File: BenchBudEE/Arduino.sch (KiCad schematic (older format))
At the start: 0 parts

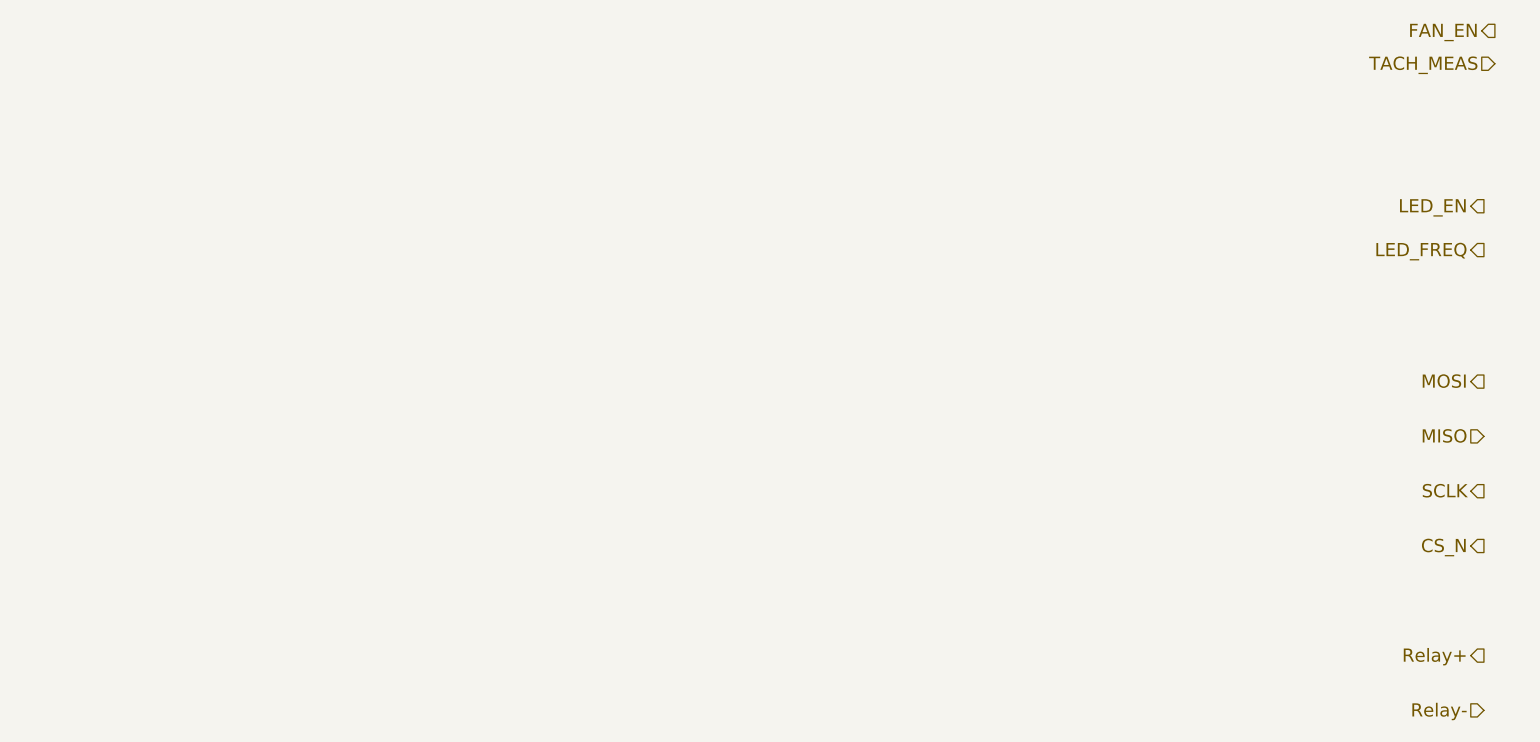
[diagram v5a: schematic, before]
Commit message: Arduino block diagram
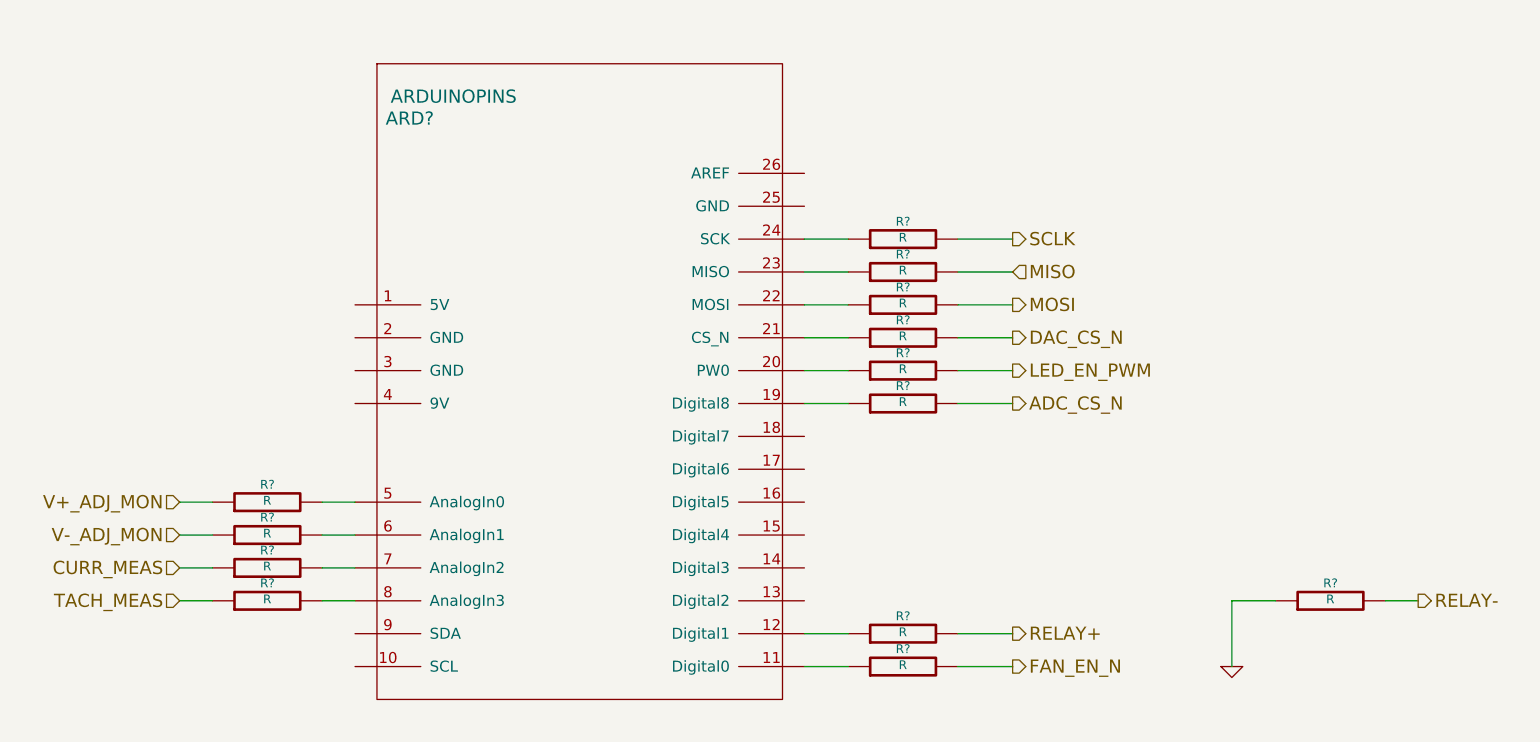
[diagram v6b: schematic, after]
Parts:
- added ARD?: ARDUINOPINS, symbol ARDUINOPINS
- added R? (x13): R, ~, symbol R
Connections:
- net MISO: now also R?.2
- net MOSI: now also R?.2
- net SCLK: now also R?.2
- net TACH_MEAS: now also R?.1
- new net: ARD?.11 (Digital0), R?.1
- new net: ARD?.12 (Digital1), R?.1
- new net: ARD?.19 (Digital8), R?.1
- new net: ARD?.20 (PW0), R?.1
- new net: ARD?.21 (CS_N), R?.1
- new net: ARD?.22 (MOSI), R?.1
- new net: ARD?.23 (MISO), R?.1
- new net: ARD?.24 (SCK), R?.1
- new net: ARD?.5 (AnalogIn0), R?.2
- new net: ARD?.6 (AnalogIn1), R?.2
- new net: ARD?.7 (AnalogIn2), R?.2
- new net: ARD?.8 (AnalogIn3), R?.2
- new net ADC_CS_N: R?.2
- new net CURR_MEAS: R?.1
- new net DAC_CS_N: R?.2
- new net FAN_EN_N: R?.2
- new net GND: R?.1
- new net LED_EN_PWM: R?.2
- new net RELAY+: R?.2
- new net RELAY-: R?.2
- new net V+_ADJ_MON: R?.1
- new net V-_ADJ_MON: R?.1

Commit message: Fan/current module refactoring
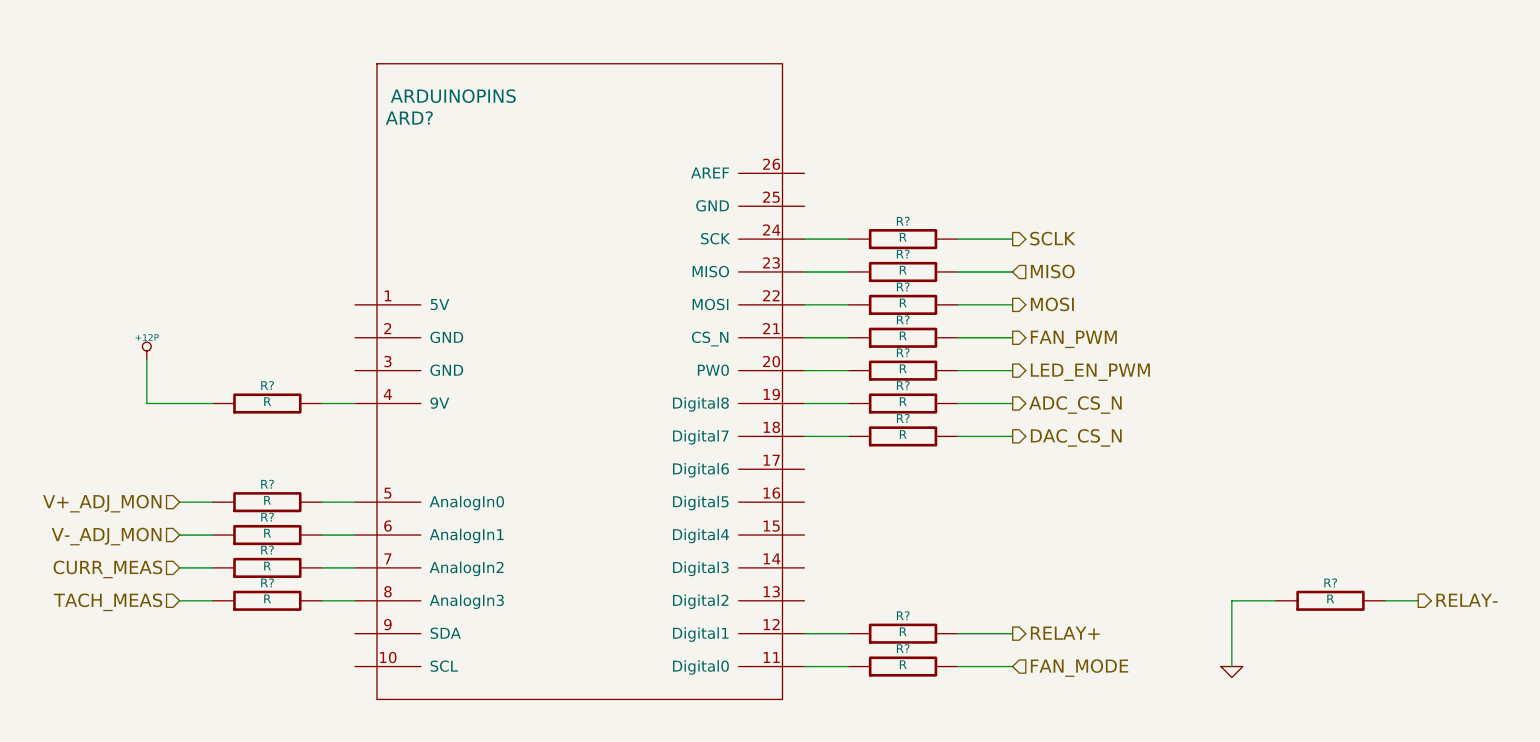
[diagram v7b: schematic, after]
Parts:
- added R? (x2): R, ~, symbol R
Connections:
- net at ARD?.11 (Digital0): now also R?.1; no longer R?.1
- net at ARD?.18 (Digital7): now also R?.1
- net at ARD?.21 (CS_N): now also R?.1; no longer R?.1
- net at ARD?.4 (9V): now also R?.2
- net FAN_EN_N renamed FAN_PWM
- new net +12P: R?.1
- new net FAN_MODE: R?.2
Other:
- moved on the sheet: R?
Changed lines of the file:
@@
 $Descr A4 11693 8268
 encoding utf-8
-Sheet 9 9
+Sheet 7 9
 Title ""
-Date "9 feb 2014"
+Date "11 feb 2014"
 Rev ""
 Comp ""
@@
 Text HLabel 6700 3900 2    60   Output ~ 0
 SCLK
+Text HLabel 6700 4800 2    60   Output ~ 0
+DAC_CS_N
 Text HLabel 6700 4350 2    60   Output ~ 0
-DAC_CS_N
-Text HLabel 6700 5850 2    60   Output ~ 0
-FAN_EN_N
+FAN_PWM
 Text HLabel 2900 5550 0    60   Input ~ 0
 TACH_MEAS
@@
 L R R?
 U 1 1 52F7E8CB
-P 6200 5850
-F 0 "R?" V 6280 5850 40  0000 C CNN
-F 1 "R" V 6207 5851 40  0000 C CNN
-F 2 "~" V 6130 5850 30  0000 C CNN
-F 3 "~" H 6200 5850 30  0000 C CNN
-	1    6200 5850
-	0    -1   -1   0
-$EndComp
-Wire Wire Line
-	5750 5850 5950 5850
-Wire Wire Line
-	6450 5850 6700 5850
+P 6200 4350
+F 0 "R?" V 6280 4350 40  0000 C CNN
+F 1 "R" V 6207 4351 40  0000 C CNN
+F 2 "~" V 6130 4350 30  0000 C CNN
+F 3 "~" H 6200 4350 30  0000 C CNN
+	1    6200 4350
+	0    -1   -1   0
+$EndComp
+Wire Wire Line
+	5750 4350 5950 4350
+Wire Wire Line
+	6450 4350 6700 4350
 $Comp
 L R R?
@@
 L R R?
 U 1 1 52F82BF7
-P 6200 4350
-F 0 "R?" V 6280 4350 40  0000 C CNN
-F 1 "R" V 6207 4351 40  0000 C CNN
-F 2 "~" V 6130 4350 30  0000 C CNN
-F 3 "~" H 6200 4350 30  0000 C CNN
-	1    6200 4350
+P 6200 4800
+F 0 "R?" V 6280 4800 40  0000 C CNN
+F 1 "R" V 6207 4801 40  0000 C CNN
+F 2 "~" V 6130 4800 30  0000 C CNN
+F 3 "~" H 6200 4800 30  0000 C CNN
+	1    6200 4800
 	0    -1   -1   0
 $EndComp
@@
 	5750 4200 5950 4200
 Wire Wire Line
-	5750 4350 5950 4350
-Wire Wire Line
-	6450 4350 6700 4350
+	5750 4800 5950 4800
+Wire Wire Line
+	6450 4800 6700 4800
 Wire Wire Line
 	6700 4200 6450 4200
@@
 Wire Wire Line
 	6450 4650 6700 4650
+Text HLabel 6700 5850 2    60   Input ~ 0
+FAN_MODE
+$Comp
+L R R?
+U 1 1 52FACCB6
+P 6200 5850
+F 0 "R?" V 6280 5850 40  0000 C CNN
+F 1 "R" V 6207 5851 40  0000 C CNN
+F 2 "~" V 6130 5850 30  0000 C CNN
+F 3 "~" H 6200 5850 30  0000 C CNN
+	1    6200 5850
+	0    -1   -1   0
+$EndComp
+Wire Wire Line
+	5750 5850 5950 5850
+Wire Wire Line
+	6450 5850 6700 5850
+$Comp
+L R R?
+U 1 1 52FACD1D
+P 3300 4650
+F 0 "R?" V 3380 4650 40  0000 C CNN
+F 1 "R" V 3307 4651 40  0000 C CNN
+F 2 "~" V 3230 4650 30  0000 C CNN
+F 3 "~" H 3300 4650 30  0000 C CNN
+	1    3300 4650
+	0    -1   -1   0
+$EndComp
+Wire Wire Line
+	3700 4650 3550 4650
+Wire Wire Line
+	3050 4650 2750 4650
+Wire Wire Line
+	2750 4650 2750 4450
+$Comp
+L +12P #PWR?
+U 1 1 52FACD63
+P 2750 4450
+F 0 "#PWR?" H 2750 4420 30  0001 C CNN
+F 1 "+12P" H 2750 4550 30  0000 C CNN
+F 2 "" H 2750 4450 60  0000 C CNN
+F 3 "" H 2750 4450 60  0000 C CNN
+	1    2750 4450
+	1    0    0    -1
+$EndComp
 $EndSCHEMATC

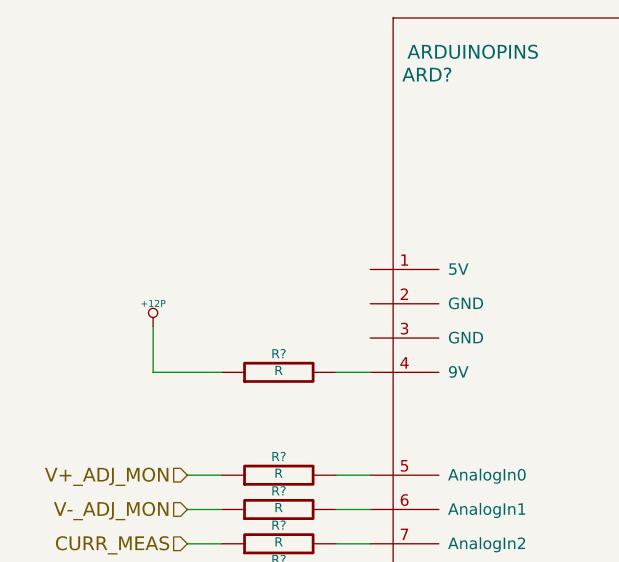
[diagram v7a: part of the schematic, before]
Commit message: PCB Outline created and changes during  components choice
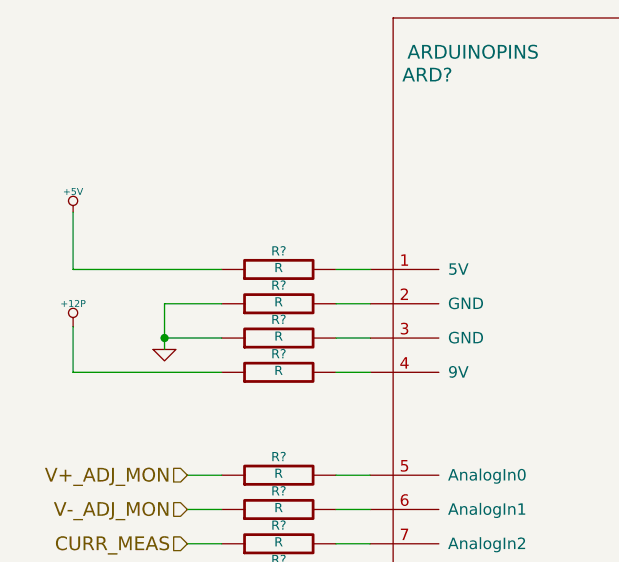
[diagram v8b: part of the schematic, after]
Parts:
- removed ARD?: ARDUINOPINS, symbol ARDUINOPINS
- added ARD?: ARDUINOPINS, ~, symbol ARDUINOPINS
- added R? (x3): R, ~, symbol R
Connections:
- net GND: now also R?.1, R?.1
- net at R?.1: now also ARD?.11 (Digital0)
- net at R?.1: now also ARD?.12 (Digital1)
- net at R?.1: now also ARD?.18 (Digital7)
- net at R?.1: now also ARD?.19 (Digital8)
- net at R?.1: now also ARD?.20 (PW0)
- net at R?.1: now also ARD?.21 (CS_N)
- net at R?.1: now also ARD?.22 (MOSI)
- net at R?.1: now also ARD?.23 (MISO)
- net at R?.1: now also ARD?.24 (SCK)
- net at R?.2: now also ARD?.4 (9V)
- net at R?.2: now also ARD?.5 (AnalogIn0)
- net at R?.2: now also ARD?.6 (AnalogIn1)
- net at R?.2: now also ARD?.7 (AnalogIn2)
- net at R?.2: now also ARD?.8 (AnalogIn3)
- new net: ARD?.1 (5V), R?.2
- new net: ARD?.2 (GND), R?.2
- new net: ARD?.3 (GND), R?.2
- new net +5V: R?.1
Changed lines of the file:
@@
 Sheet 7 9
 Title ""
-Date "11 feb 2014"
+Date "16 feb 2014"
 Rev ""
 Comp ""
@@
 Text HLabel 2900 5550 0    60   Input ~ 0
 TACH_MEAS
-$Comp
-L ARDUINOPINS ARD?
-U 1 1 52F7E894
-P 4750 4650
-F 0 "ARD?" H 3950 5950 60  0000 C CNN
-F 1 "ARDUINOPINS" H 4150 6050 60  0000 C CNN
-F 2 "" H 4450 3700 60  0000 C CNN
-F 3 "" H 4450 3700 60  0000 C CNN
-	1    4750 4650
-	1    0    0    -1
-$EndComp
 Text HLabel 2900 5400 0    60   Input ~ 0
 CURR_MEAS
@@
 	3700 4650 3550 4650
 Wire Wire Line
-	3050 4650 2750 4650
-Wire Wire Line
-	2750 4650 2750 4450
+	3050 4650 2400 4650
+Wire Wire Line
+	2400 4650 2400 4450
 $Comp
 L +12P #PWR?
 U 1 1 52FACD63
-P 2750 4450
-F 0 "#PWR?" H 2750 4420 30  0001 C CNN
-F 1 "+12P" H 2750 4550 30  0000 C CNN
-F 2 "" H 2750 4450 60  0000 C CNN
-F 3 "" H 2750 4450 60  0000 C CNN
-	1    2750 4450
-	1    0    0    -1
-$EndComp
+P 2400 4450
+F 0 "#PWR?" H 2400 4420 30  0001 C CNN
+F 1 "+12P" H 2400 4550 30  0000 C CNN
+F 2 "" H 2400 4450 60  0000 C CNN
+F 3 "" H 2400 4450 60  0000 C CNN
+	1    2400 4450
+	1    0    0    -1
+$EndComp
+$Comp
+L ARDUINOPINS ARD?
+U 1 1 52FF78C8
+P 4750 4650
+F 0 "ARD?" H 3950 5950 60  0000 C CNN
+F 1 "ARDUINOPINS" H 4150 6050 60  0000 C CNN
+F 2 "~" H 4450 3700 60  0000 C CNN
+F 3 "~" H 4450 3700 60  0000 C CNN
+	1    4750 4650
+	1    0    0    -1
+$EndComp
+Wire Wire Line
+	2400 4200 2400 3950
+$Comp
+L +5V #PWR?
+U 1 1 5300B8CD
+P 2400 3950
+F 0 "#PWR?" H 2400 4040 20  0001 C CNN
+F 1 "+5V" H 2400 4040 30  0000 C CNN
+F 2 "" H 2400 3950 60  0000 C CNN
+F 3 "" H 2400 3950 60  0000 C CNN
+	1    2400 3950
+	1    0    0    -1
+$EndComp
+$Comp
+L R R?
+U 1 1 5300B8E0
+P 3300 4200
+F 0 "R?" V 3380 4200 40  0000 C CNN
+F 1 "R" V 3307 4201 40  0000 C CNN
+F 2 "~" V 3230 4200 30  0000 C CNN
+F 3 "~" H 3300 4200 30  0000 C CNN
+	1    3300 4200
+	0    -1   -1   0
+$EndComp
+$Comp
+L R R?
+U 1 1 5300B8E6
+P 3300 4350
+F 0 "R?" V 3380 4350 40  0000 C CNN
+F 1 "R" V 3307 4351 40  0000 C CNN
+F 2 "~" V 3230 4350 30  0000 C CNN
+F 3 "~" H 3300 4350 30  0000 C CNN
+	1    3300 4350
+	0    -1   -1   0
+$EndComp
+$Comp
+L R R?
+U 1 1 5300B8EC
+P 3300 4500
+F 0 "R?" V 3380 4500 40  0000 C CNN
+F 1 "R" V 3307 4501 40  0000 C CNN
+F 2 "~" V 3230 4500 30  0000 C CNN
+F 3 "~" H 3300 4500 30  0000 C CNN
+	1    3300 4500
+	0    -1   -1   0
+$EndComp
+Wire Wire Line
+	3550 4200 3700 4200
+Wire Wire Line
+	3700 4350 3550 4350
+Wire Wire Line
+	3700 4500 3550 4500
+Wire Wire Line
+	3050 4200 2400 4200
+Wire Wire Line
+	3050 4350 2800 4350
+Wire Wire Line
+	2800 4350 2800 4550
+Wire Wire Line
+	2800 4500 3050 4500
+Connection ~ 2800 4500
+$Comp
+L GND #PWR?
+U 1 1 5300B9FD
+P 2800 4550
+F 0 "#PWR?" H 2800 4550 30  0001 C CNN
+F 1 "GND" H 2800 4480 30  0001 C CNN
+F 2 "" H 2800 4550 60  0000 C CNN
+F 3 "" H 2800 4550 60  0000 C CNN
+	1    2800 4550
+	1    0    0    -1
+$EndComp
